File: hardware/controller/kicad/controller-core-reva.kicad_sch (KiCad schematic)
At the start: 215 parts, among them J101 12V_ISOLATED_INPUT / JST XH, J102 STM_SWD / 1x6 2.54mm, J103 ESP_UART / 1x6 2.54mm, J104 UI_LINK / WR-MM 16, J105 JP13 NTC / 2 vías, J106 JP5 FLOW ADAPTER / VCC-GND-OC, J107 JP14 DOOR / contacto seco, J108 JP16 VISUAL V1..V8 / XH-8, J109 JP22 WATER / RED-WHITE-BLACK, J110 USB-C SERVICE / USB 2.0, J111 USB BENCH POWER / OPEN, J112 24V_ACTUATOR_INPUT / JST XH, J113 JP3 VALVE / A2506, J114 POWER PROBE / MEASURE ONLY, J115 JP8 GRINDER / 320VDC, J116 JP19 HEATER / 1900W 27R5, J117 JP24 PUMP / 230VAC, J118 JP17 MAINS / L-N, J119 JP1 PE TO BOILER, J120 JP9 PE INPUT, J121 24V INTERNAL SELECT / OPEN FO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, K701 G5RL-1A-E-TV8 DC24, Q501 SI2308A, Q701 BSS138LT1G / relay coil, Q703 BTA24-800BWRG / heater, Q704 BTA24-800BWRG / pump, Q705 BSS138LT1G / heater opto LED, Q706 BSS138LT1G / pump opto LED, Q707 BSS138LT1G / grinder opto LED, Q708 BTA24-800BWRG / grinder, U101 STM32G431RBT6, U201 ESP32-S3-WROOM-1U-N8R8, U203 USBLC6-2SC6, U301 AP63203WU-7, U302 TPS2553DBVR / UI 0.5A limit, U303 AP63200WU-7 / 24V to 12V, U304 TPS2553DBVR / JP22 0.13A limit, U501 DRV8876PWPR, U502 UCC27517DBVR, U601 TPS3828-33DBVR, U602 SN74LVC2G08DCTR, U603 SN74LVC2G08DCTR, U604 SN74LVC2G08DCTR, U605 SN74LVC1G17DBVR, U606 SN74LVC1G132DBVR, U701 MOC3083 / zero-cross, U702 MOC3083 / zero-cross, U703 MOC3083 / zero-cross, U704 TMCS1133B4AQDVGR / grinder cu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

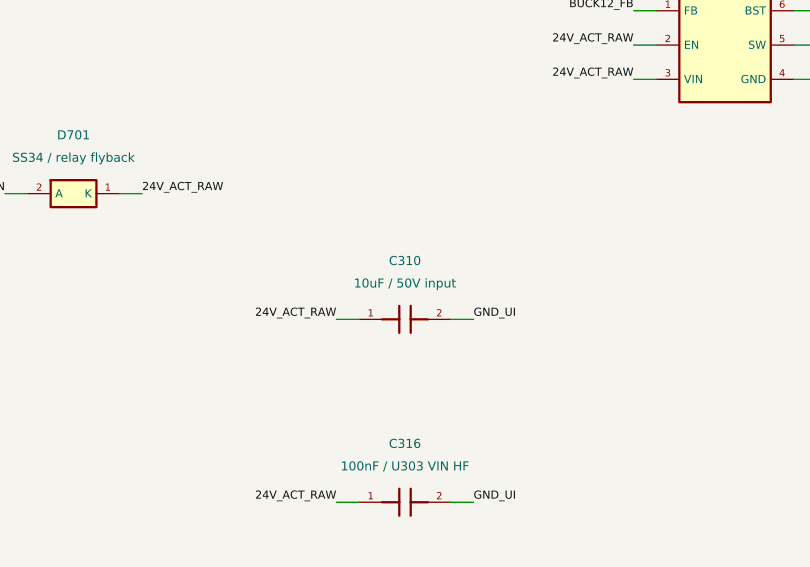
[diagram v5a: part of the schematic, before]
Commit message: Make C310 a 1210 to keep its capacitance at 24 V
Samsung's Component Library DC-bias curves (25 C, 1 Vrms, 1 kHz, read
2026-10-07) give the 10 uF/50 V X7R 1206 that was C310 only 2.27 uF at
24 V, and the 1210 CL32B106KBJNNNE (C138687) 4.8 uF: twice the effective
input capacitance for U303. C315 stays a 1206: at 12 V it keeps 5.0 uF,
2.5 times what the 0805 C301 keeps (2.0 uF). That corrects the issue #3
note that a quarter of the rated voltage kept most of the capacitance.

C310 moves to (122.5, 9.85) with its feed and ground via adjusted; its
courtyard reaches y = 11.5 mm, so the silkscreen logo moves 0.5 mm down.
The catalogue records the curve readings for both parts.

ERC 0 on both boards; DRC with all severities 0 violations, 0
unconnected, parity only MH1-MH3; check_controller_pcb --self-test
passes; board model 0 errors, 0 warnings; tests/sim 94/94; CTest 3/3.

Co-Authored-By: Claude Opus 5.5 <noreply@anthropic.com>
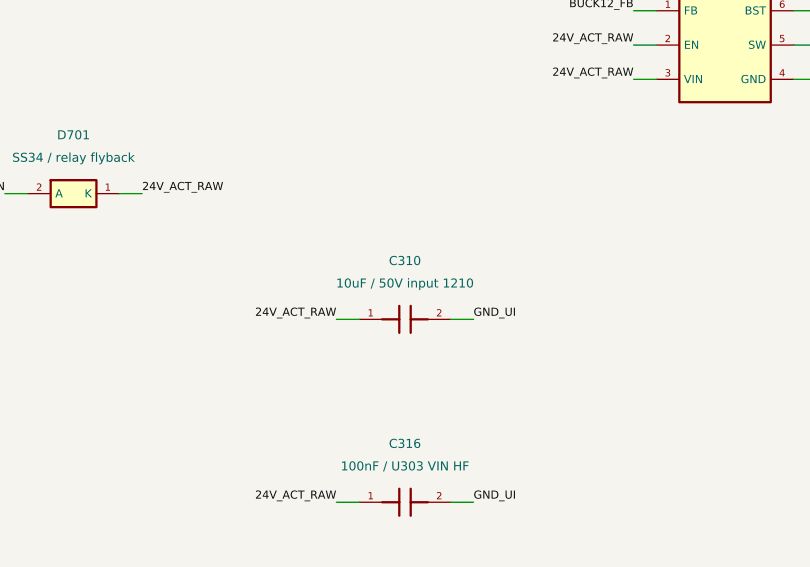
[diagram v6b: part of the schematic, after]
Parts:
- C310: value 10uF / 50V input -> 10uF / 50V input 1210; footprint Capacitor_SMD:C_1206_3216Metric -> Capacitor_SMD:C_1210_3225Metric; lcsc C89632 -> C138687; mpn CL31B106KBHNNNE -> CL32B106KBJNNNE

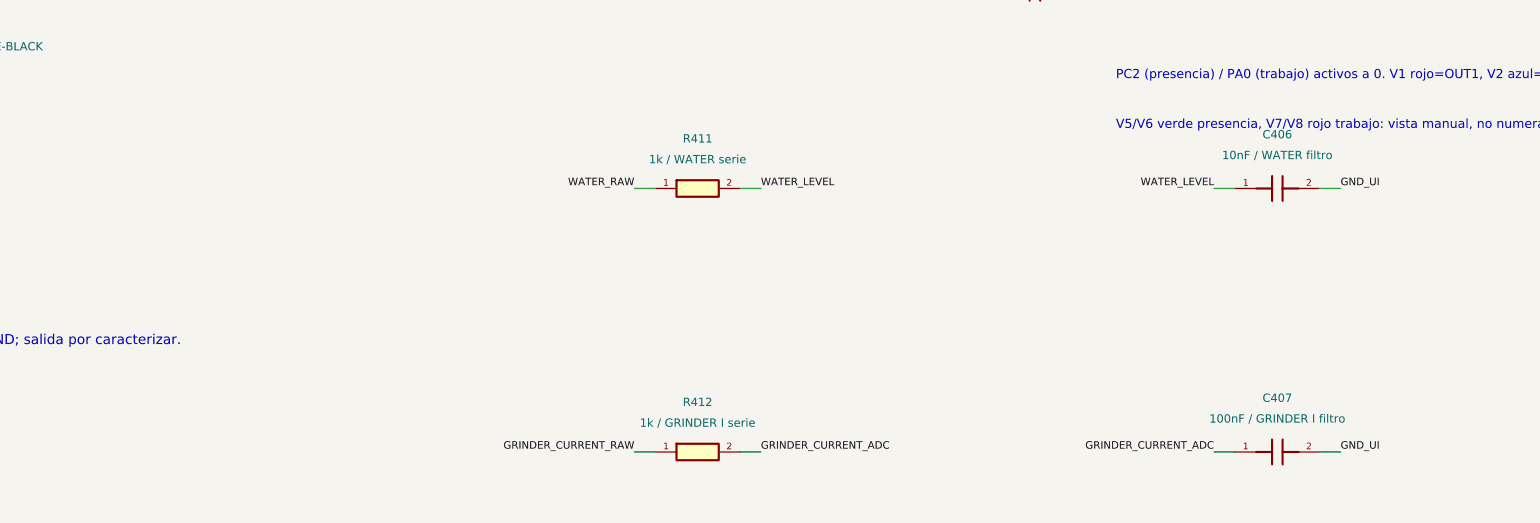
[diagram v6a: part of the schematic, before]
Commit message: Reserve DNP footprints for a JP22 bias resistor
With JP22 unplugged PC3 floats (issue #7). Which bias it needs depends on
the sensor output that WL-01 has not measured yet, so both options get a
footprint and neither is fitted: R415 pulls WATER_RAW up to WATER_VCC (open
collector) and R416 pulls it down to GND (push-pull), 100k 0603 in line
above J109.

The generator takes dnp=True and the footprint carries KiCad's DNP
attribute; the simulator now leaves DNP parts out of the circuit, with a
test that fails if it loads them again.

Refs #7

Co-Authored-By: Claude Opus 5.5 <noreply@anthropic.com>
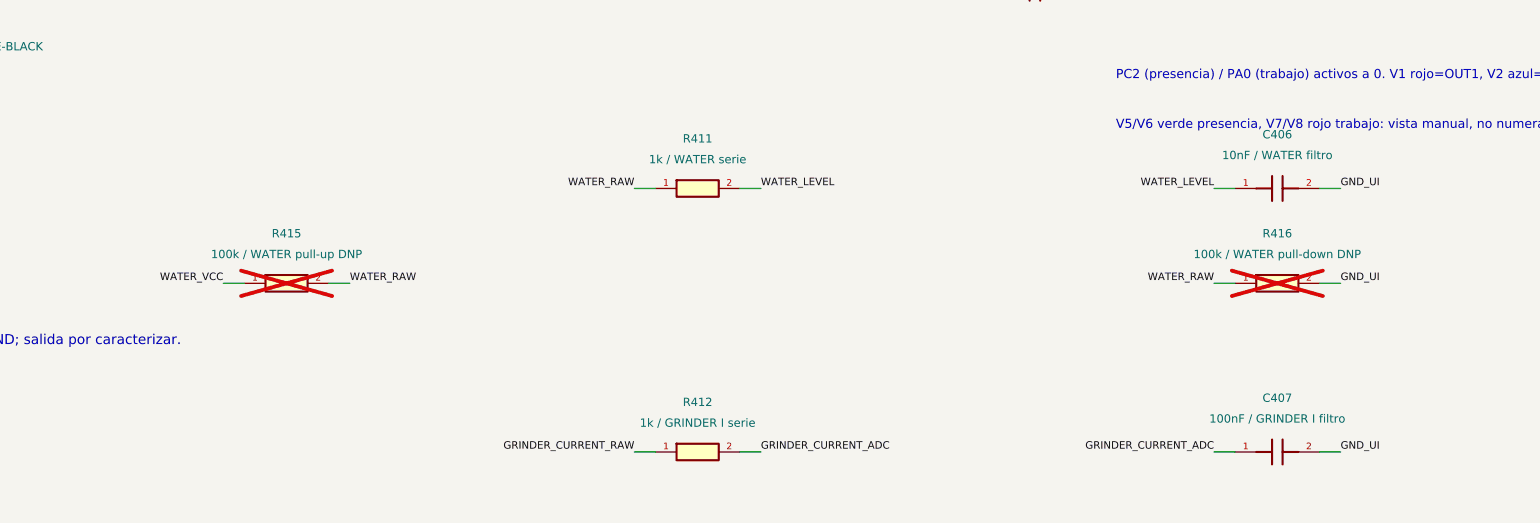
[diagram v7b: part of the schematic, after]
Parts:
- added R415: 100k / WATER pull-up DNP, Resistor_SMD:R_0603_1608Metric, symbol OpenSaeco:R
- added R416: 100k / WATER pull-down DNP, Resistor_SMD:R_0603_1608Metric, symbol OpenSaeco:R
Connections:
- net GND_UI: now also R416.2
- net WATER_RAW: now also R415.2, R416.1
- net WATER_VCC: now also R415.1

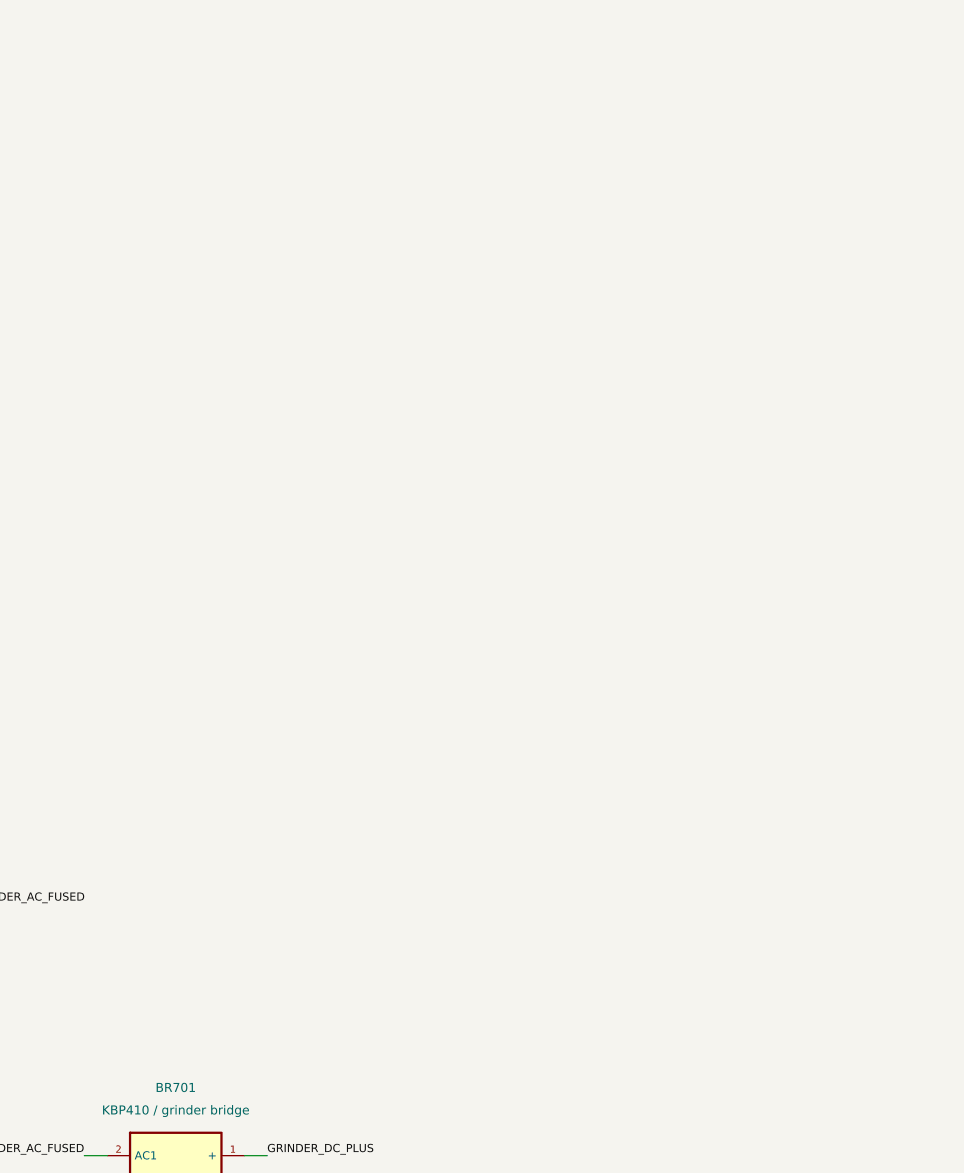
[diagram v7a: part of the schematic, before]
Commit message: Reserve DNP footprints for RC snubbers on Q704 and Q708
The pump and grinder triacs have no snubber until PU-03 and GR-05 measure
the turn-off dV/dt, and there was no room to add one without a new board.
Both now have an unfitted RC across A1-A2 on the bottom side, under the
heatsink foot: C705/R727 above Q704 where B.Cu was free, and C706/R728 in
a notch cut out of the south-west corner of the B.Cu LOAD_L_ENABLED block.
The heater still comes down x = 70.5-77.6 mm of that block; about 2 A of
its 8.4 A is estimated to move onto the F.Cu lane west of the notch.

The layout script places footprints on the bottom side, the snubber nets
are Mains class, check_controller_core.py asserts their nets, and the
export no longer lists DNP parts as open before ordering.

Co-Authored-By: Claude Opus 5.5 <noreply@anthropic.com>
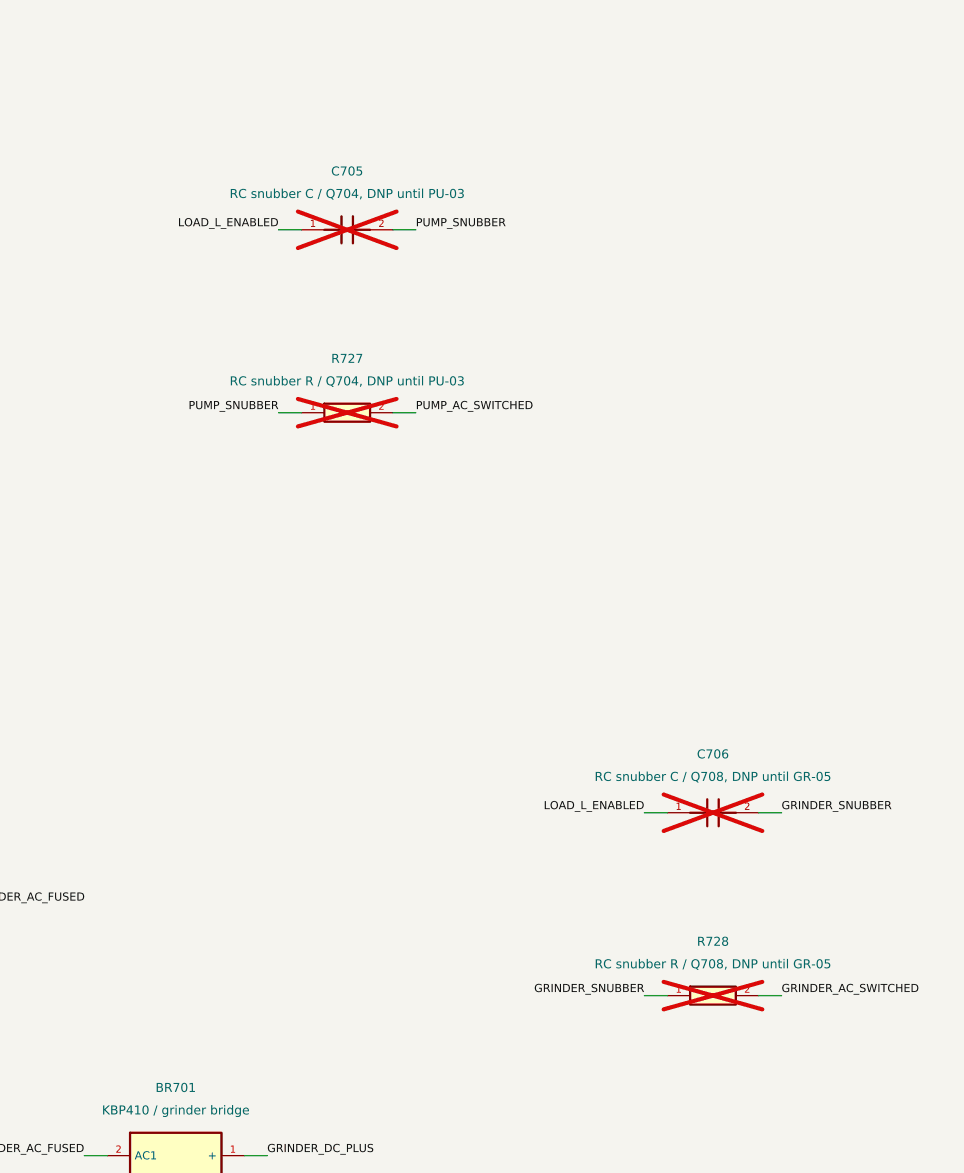
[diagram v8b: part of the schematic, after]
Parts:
- added C705: RC snubber C / Q704, DNP until PU-03, Capacitor_SMD:C_1812_4532Metric, symbol OpenSaeco:C
- added C706: RC snubber C / Q708, DNP until GR-05, Capacitor_SMD:C_1812_4532Metric, symbol OpenSaeco:C
- added R727: RC snubber R / Q704, DNP until PU-03, Resistor_SMD:R_2512_6332Metric, symbol OpenSaeco:R
- added R728: RC snubber R / Q708, DNP until GR-05, Resistor_SMD:R_2512_6332Metric, symbol OpenSaeco:R
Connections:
- net GRINDER_AC_SWITCHED: now also R728.2
- net LOAD_L_ENABLED: now also C705.1, C706.1
- net PUMP_AC_SWITCHED: now also R727.2
- new net GRINDER_SNUBBER: C706.2, R728.1
- new net PUMP_SNUBBER: C705.2, R727.1
